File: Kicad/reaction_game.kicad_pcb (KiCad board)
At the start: 2 copper layers, 95 x 67.5 mm, 11 parts, among them SW1 Player 1, SW2 Player 2, U1 RaspberryPico

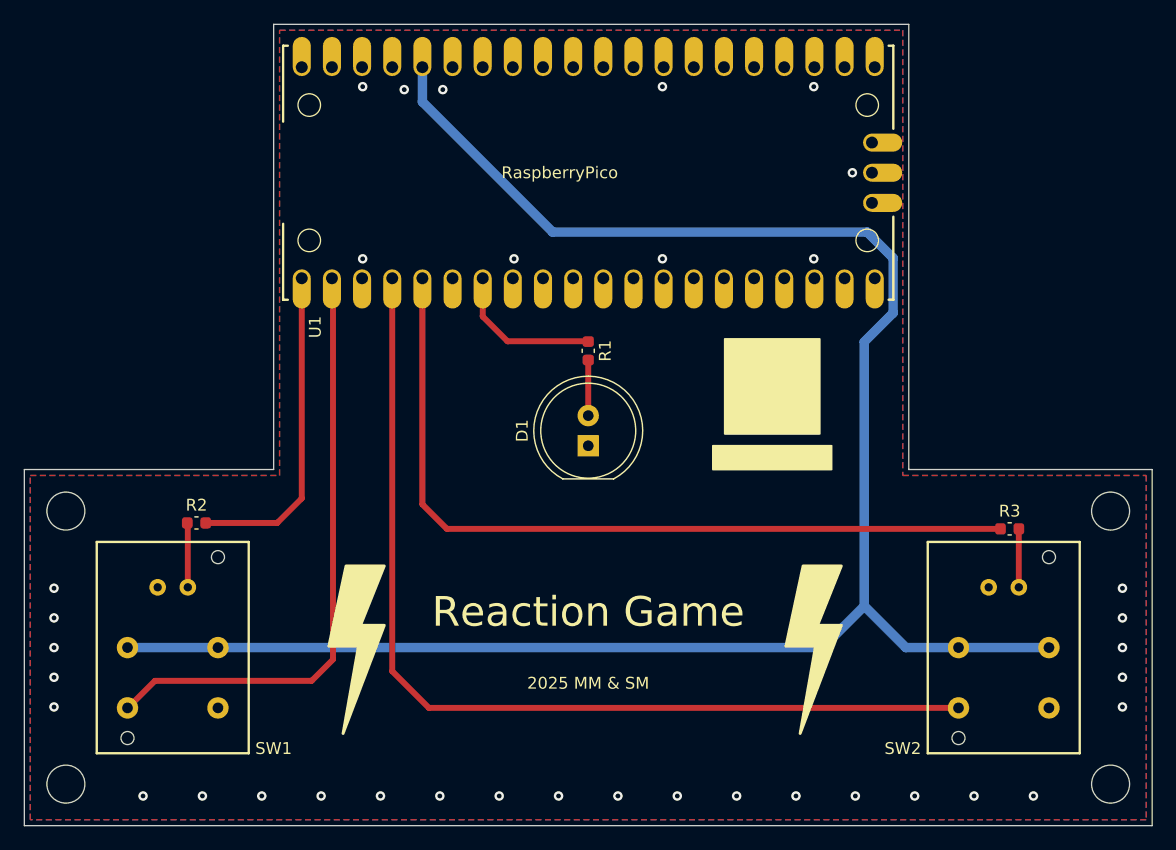
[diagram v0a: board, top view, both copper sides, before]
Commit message: Fixed Pico
- flipped pico
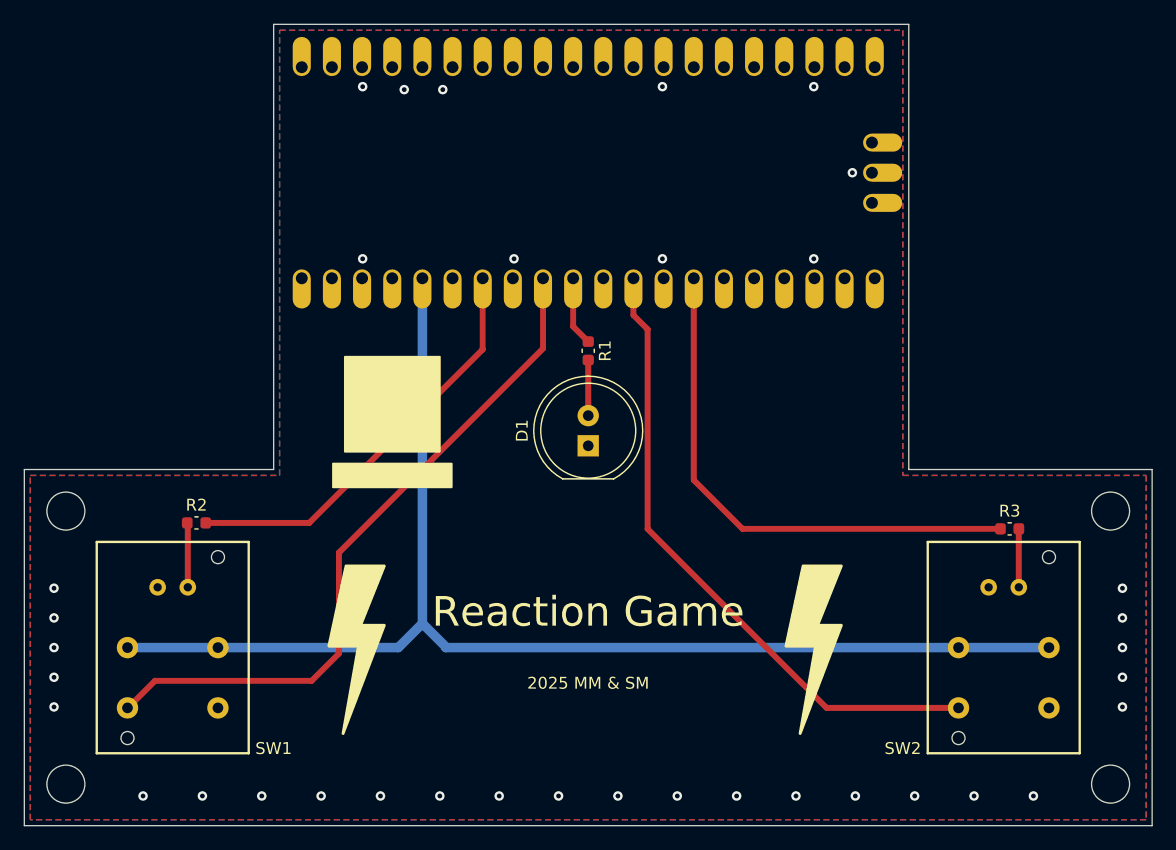
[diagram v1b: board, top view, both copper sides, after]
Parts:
- U1: moved to B.Cu
- turned U1 to -90 degrees
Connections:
- U1 pad 1: /LED_1 -> unconnected-(U1-GP0/SPI0_RX/I2C0_SDA/UART0_TX-Pad1)
- U1 pad 2: /Button_1 -> unconnected-(U1-GP1/SPI0_CSn/I2C0_SCL/UART0_RX-Pad2)
- U1 pad 27: unconnected-(U1-GP21/I2C0_SCL-Pad27) -> /LED_2
- U1 pad 29: unconnected-(U1-GP22-Pad29) -> /Button_2
- U1 pad 31: unconnected-(U1-GP26/ADC0/I2C1_SDA-Pad31) -> /Game_LED
- U1 pad 32: unconnected-(U1-GP27/ADC1/I2C1_SCL-Pad32) -> /Button_1
- U1 pad 34: unconnected-(U1-GP28/ADC2-Pad34) -> /LED_1
- U1 pad 4: /Button_2 -> unconnected-(U1-GP2/SPI0_SCK/I2C1_SDA-Pad4)
- U1 pad 5: /LED_2 -> unconnected-(U1-GP3/SPI0_TX/I2C1_SCL-Pad5)
- U1 pad 7: /Game_LED -> unconnected-(U1-GP5/SPI0_CSn/I2C0_SCL/UART1_RX-Pad7)
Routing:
- net +3V3: track 158.9 -> 108.4 mm
- net /Button_2: track 82.1 -> 54.0 mm
- net /LED_2: track 68.6 -> 44.5 mm
- net /LED_1: track 27.5 -> 35.4 mm
- net /Button_1: track 51.1 -> 58.4 mm
- net /Game_LED: track 13.0 -> 5.86 mm

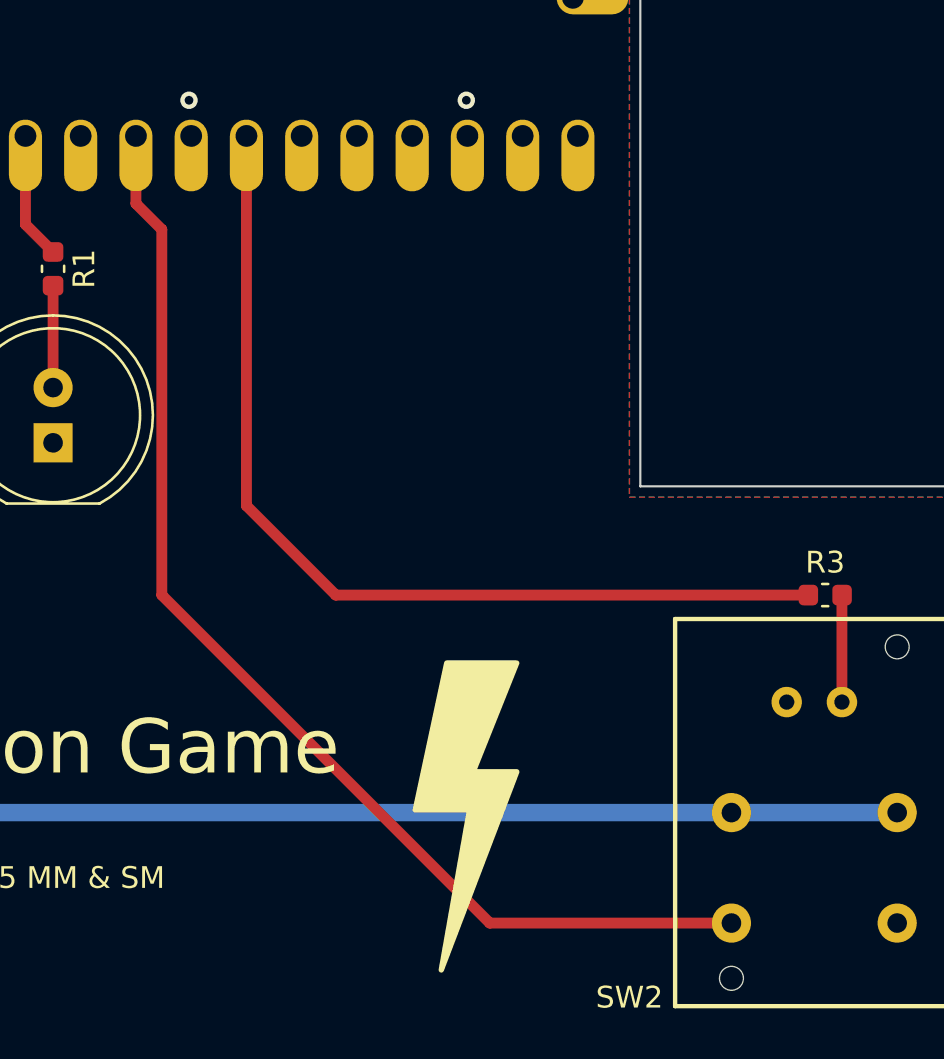
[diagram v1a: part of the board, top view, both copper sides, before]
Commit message: Pin change
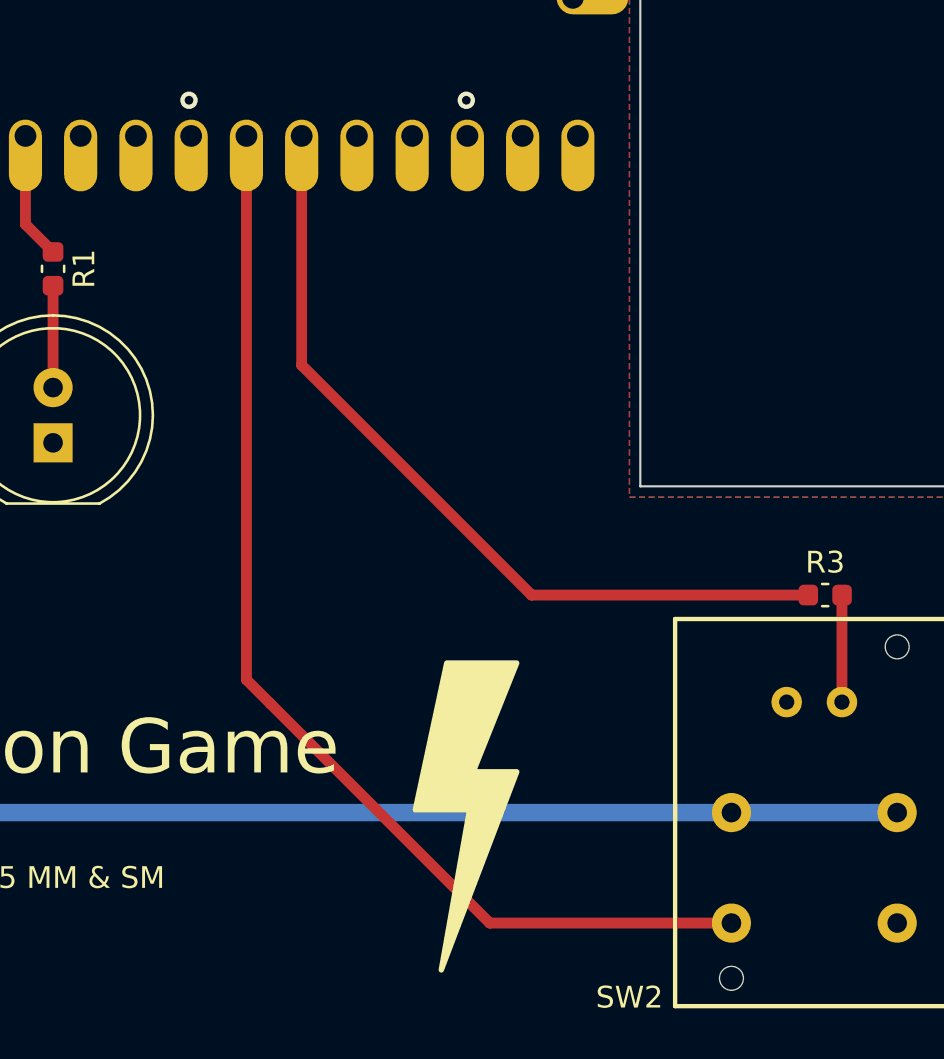
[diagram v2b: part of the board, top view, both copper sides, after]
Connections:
- U1 pad 26: unconnected-(U1-GP20/I2C0_SDA-Pad26) -> /LED_2
- U1 pad 27: /LED_2 -> /Button_2
- U1 pad 29: /Button_2 -> unconnected-(U1-GP22-Pad29)
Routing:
- net /LED_2: track 44.5 -> 38.2 mm
- net /Button_2: track 54.0 -> 51.9 mm
